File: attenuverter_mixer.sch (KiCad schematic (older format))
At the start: 77 parts, among them J0 Eurorack power, J1 In 1, J10 AudioJack1_SwitchT, J2 Out 1, J3 AudioJack1_SwitchT, J4 Out 2, J5 AudioJack1_SwitchT, J6 Out 3, J7 AudioJack1_SwitchT, J8 Out 4, J9 AudioJack1_SwitchT, U1 TL074, U2 TL074, U3 TL074

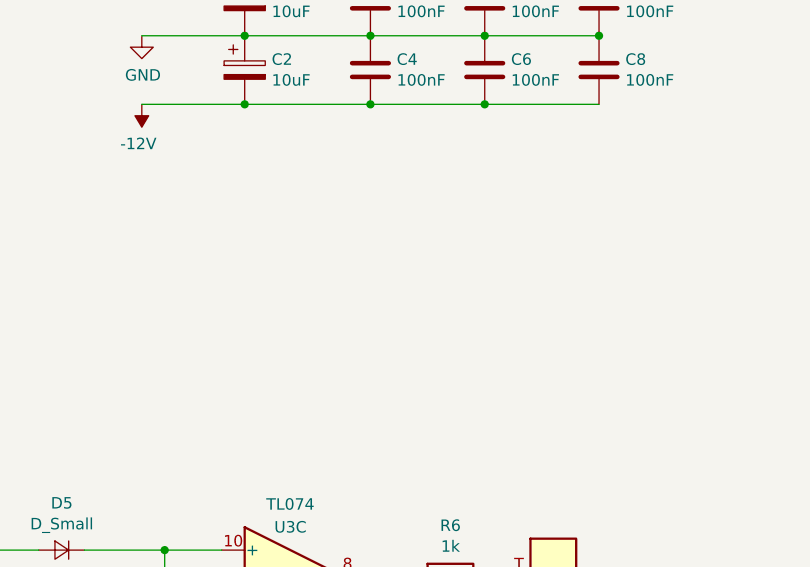
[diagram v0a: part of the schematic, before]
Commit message: Add the missing 5v voltage reference
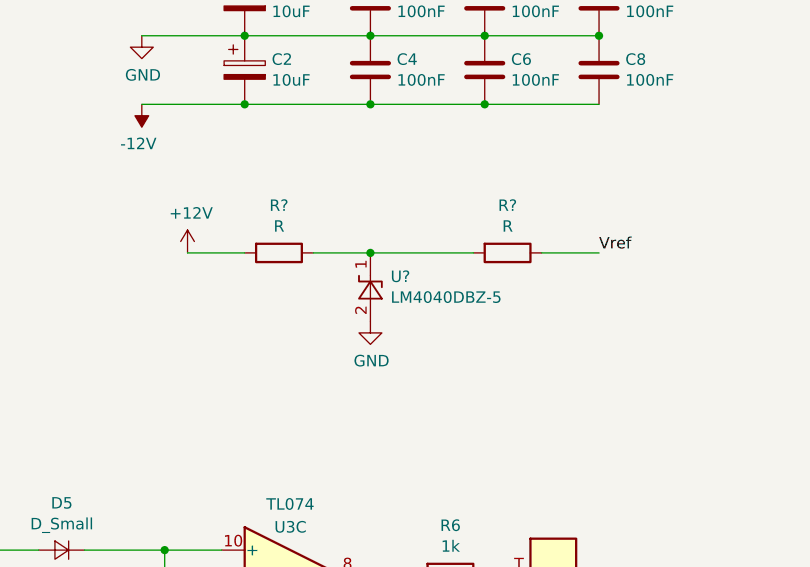
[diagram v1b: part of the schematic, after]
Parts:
- added R? (x2): R, symbol Device:R
- added U?: LM4040DBZ-5, Package_TO_SOT_SMD:SOT-23, symbol Reference_Voltage:LM4040DBZ-5
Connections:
- net +12V: now also R?.2
- net GND: now also U?.2 (A)
- net Vref: now also R?.1
- new net: R?.1, R?.2, U?.1 (K)
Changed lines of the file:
@@
 EESchema Schematic File Version 4
+LIBS:attenuverter_mixer-cache
 EELAYER 30 0
 EELAYER END
@@
 	0    -1   -1   0
 $EndComp
+$Comp
+L Reference_Voltage:LM4040DBZ-5 U?
+U 1 1 5D806F7C
+P 9350 3300
+F 0 "U?" V 9396 3212 50  0000 R CNN
+F 1 "LM4040DBZ-5" V 9305 3212 50  0000 R CNN
+F 2 "Package_TO_SOT_SMD:SOT-23" H 9350 3100 50  0001 C CIN
+F 3 "http://www.ti.com/lit/ds/symlink/lm4040-n.pdf" H 9350 3300 50  0001 C CIN
+	1    9350 3300
+	0    -1   -1   0
+$EndComp
+$Comp
+L power:GND #PWR?
+U 1 1 5D83B38C
+P 9350 3450
+F 0 "#PWR?" H 9350 3200 50  0001 C CNN
+F 1 "GND" H 9355 3277 50  0000 C CNN
+F 2 "" H 9350 3450 50  0001 C CNN
+F 3 "" H 9350 3450 50  0001 C CNN
+	1    9350 3450
+	1    0    0    -1
+$EndComp
+$Comp
+L power:+12V #PWR?
+U 1 1 5D851100
+P 8550 3150
+F 0 "#PWR?" H 8550 3000 50  0001 C CNN
+F 1 "+12V" H 8565 3323 50  0000 C CNN
+F 2 "" H 8550 3150 50  0001 C CNN
+F 3 "" H 8550 3150 50  0001 C CNN
+	1    8550 3150
+	1    0    0    -1
+$EndComp
+$Comp
+L Device:R R?
+U 1 1 5D89B833
+P 8950 3150
+F 0 "R?" V 8743 3150 50  0000 C CNN
+F 1 "R" V 8834 3150 50  0000 C CNN
+F 2 "" V 8880 3150 50  0001 C CNN
+F 3 "~" H 8950 3150 50  0001 C CNN
+	1    8950 3150
+	0    1    1    0
+$EndComp
+Wire Wire Line
+	8800 3150 8550 3150
+Wire Wire Line
+	9100 3150 9350 3150
+$Comp
+L Device:R R?
+U 1 1 5D8BBE6D
+P 9950 3150
+F 0 "R?" V 9743 3150 50  0000 C CNN
+F 1 "R" V 9834 3150 50  0000 C CNN
+F 2 "" V 9880 3150 50  0001 C CNN
+F 3 "~" H 9950 3150 50  0001 C CNN
+	1    9950 3150
+	0    1    1    0
+$EndComp
+Wire Wire Line
+	9350 3150 9800 3150
+Connection ~ 9350 3150
+Text Label 10350 3150 0    50   ~ 0
+Vref
+Wire Wire Line
+	10100 3150 10350 3150
 $EndSCHEMATC

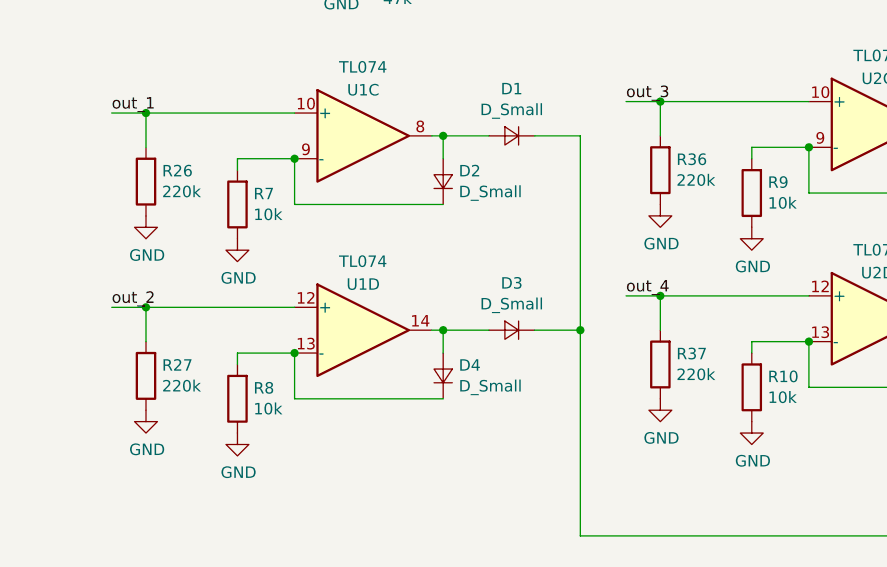
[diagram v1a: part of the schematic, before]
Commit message: Adjust peaks pull down resistors up to 1M
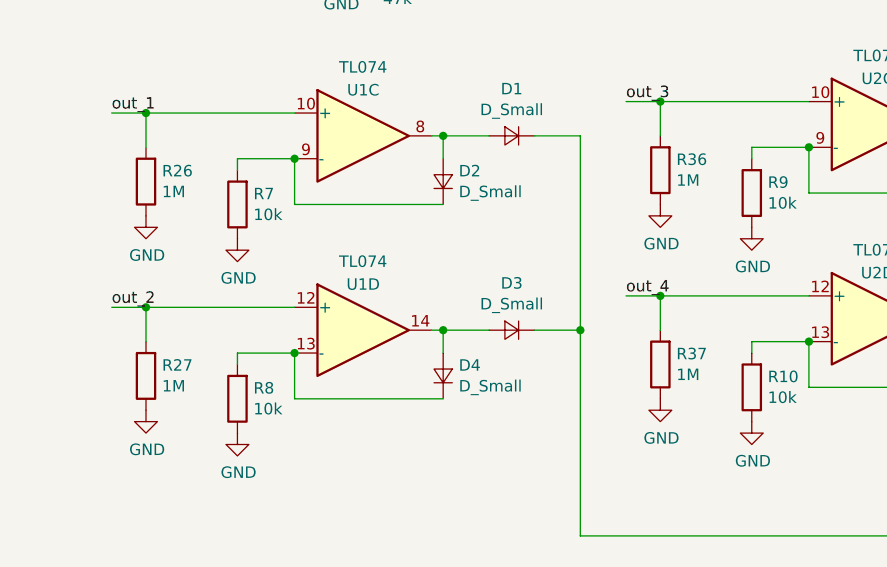
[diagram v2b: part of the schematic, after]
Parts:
- R26, R27, R36, R37: value 220k -> 1M
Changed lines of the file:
@@
 P 4150 4700
 F 0 "R26" H 4080 4654 50  0000 R CNN
-F 1 "220k" H 4080 4745 50  0000 R CNN
+F 1 "1M" H 4080 4745 50  0000 R CNN
 F 2 "" V 4080 4700 50  0001 C CNN
 F 3 "~" H 4150 4700 50  0001 C CNN
@@
 P 4150 5550
 F 0 "R27" H 4080 5504 50  0000 R CNN
-F 1 "220k" H 4080 5595 50  0000 R CNN
+F 1 "1M" H 4080 5595 50  0000 R CNN
 F 2 "" V 4080 5550 50  0001 C CNN
 F 3 "~" H 4150 5550 50  0001 C CNN
@@
 P 6400 4650
 F 0 "R36" H 6330 4604 50  0000 R CNN
-F 1 "220k" H 6330 4695 50  0000 R CNN
+F 1 "1M" H 6330 4695 50  0000 R CNN
 F 2 "" V 6330 4650 50  0001 C CNN
 F 3 "~" H 6400 4650 50  0001 C CNN
@@
 P 6400 5500
 F 0 "R37" H 6330 5454 50  0000 R CNN
-F 1 "220k" H 6330 5545 50  0000 R CNN
+F 1 "1M" H 6330 5545 50  0000 R CNN
 F 2 "" V 6330 5500 50  0001 C CNN
 F 3 "~" H 6400 5500 50  0001 C CNN

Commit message: assorted updates
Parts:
- removed D1, D2, D3, D4, D5, D6, D7, D8: D_Small, symbol Device:D_Small
- removed unit 2 of U1
- removed unit 3 of U1
- removed unit 4 of U1
- removed unit 1 of U2
- removed unit 2 of U2
- removed unit 3 of U2
- removed unit 4 of U2
- removed unit 3 of U3
- removed unit 5 of U3
- removed unit 4 of U3
- added C16, C9: 100nF, Capacitor_THT:C_Disc_D3.0mm_W1.6mm_P2.50mm, symbol Device:C
- added D1, D12, D13, D18, D2, D3, D4, D5, D6, D7: D_TVS, Diode_THT:D_DO-15_P12.70mm_Horizontal, symbol Device:D_TVS
- added D10, D11, D14, D15, D8, D9: 1N4148, Diode_THT:D_DO-35_SOD27_P7.62mm_Horizontal, symbol Diode:1N4148
- added D16, D17: 1N5817, Diode_THT:D_DO-41_SOD81_P10.16mm_Horizontal, symbol Device:D_Schottky
- added R38: 47k, Resistor_THT:R_Axial_DIN0207_L6.3mm_D2.5mm_P10.16mm_Horizontal, symbol Device:R
- added R39, R40, R41, R42: 100k, Resistor_THT:R_Axial_DIN0207_L6.3mm_D2.5mm_P10.16mm_Horizontal, symbol Device:R
- added R43, R44, R48: 330R, Resistor_THT:R_Axial_DIN0309_L9.0mm_D3.2mm_P12.70mm_Horizontal, symbol Device:R
- added R45, R46: 220k, Resistor_THT:R_Axial_DIN0207_L6.3mm_D2.5mm_P10.16mm_Horizontal, symbol Device:R
- added RV5, RV6: 100k, Potentiometer_THT:Potentiometer_Alpha_RD901F-40-00D_Single_Vertical, symbol Device:R_POT
- added unit 2 of U1
- added unit 2 of U2
- added unit 1 of U2
- added U3, U4: TL072, Package_SO:SOIC-8_3.9x4.9mm_P1.27mm, symbol Amplifier_Operational:TL072
- added unit 4 of U5
- added unit 5 of U5
- added unit 3 of U5
- C1, C2: footprint (none) -> Capacitor_THT:CP_Radial_D5.0mm_P2.00mm
- C10, C14, C15: footprint (none) -> Capacitor_THT:C_Disc_D3.0mm_W2.0mm_P2.50mm
- C11, C12, C13: value 18pF -> 100nF; footprint (none) -> Capacitor_THT:C_Disc_D3.0mm_W1.6mm_P2.50mm
- C3, C4, C8: footprint (none) -> Capacitor_THT:C_Disc_D3.0mm_W1.6mm_P2.50mm
- C5, C6, C7: value 100nF -> 18pF; footprint (none) -> Capacitor_THT:C_Disc_D3.0mm_W2.0mm_P2.50mm
- J0: footprint Connector_IDC:IDC-Header_2x05_P2.54mm_Vertical_Lock -> Connector_PinSocket_2.54mm:PinSocket_2x05_P2.54mm_Vertical
- J1: value In 1 -> Input; footprint (none) -> kicad_libraries:Jack_3.5mm_QingPu_WQP-PJ398SM_Vertical_CircularHoles
- J10: value AudioJack1_SwitchT -> Or out; footprint (none) -> kicad_libraries:Jack_3.5mm_QingPu_WQP-PJ398SM_Vertical_CircularHoles
- J2: value Out 1 -> Out; footprint (none) -> kicad_libraries:Jack_3.5mm_QingPu_WQP-PJ398SM_Vertical_CircularHoles
- J3, J5: value AudioJack1_SwitchT -> Input; footprint (none) -> kicad_libraries:Jack_3.5mm_QingPu_WQP-PJ398SM_Vertical_CircularHoles
- J4: value Out 2 -> Out; footprint (none) -> kicad_libraries:Jack_3.5mm_QingPu_WQP-PJ398SM_Vertical_CircularHoles
- J6: value Out 3 -> Input; footprint (none) -> kicad_libraries:Jack_3.5mm_QingPu_WQP-PJ398SM_Vertical_CircularHoles
- J7: value AudioJack1_SwitchT -> Out; footprint (none) -> kicad_libraries:Jack_3.5mm_QingPu_WQP-PJ398SM_Vertical_CircularHoles
- J8: value Out 4 -> Out; footprint (none) -> kicad_libraries:Jack_3.5mm_QingPu_WQP-PJ398SM_Vertical_CircularHoles
- J9: value AudioJack1_SwitchT -> Sum out; footprint (none) -> kicad_libraries:Jack_3.5mm_QingPu_WQP-PJ398SM_Vertical_CircularHoles
- R1, R5: value 1k -> 330R; footprint (none) -> Resistor_THT:R_Axial_DIN0309_L9.0mm_D3.2mm_P12.70mm_Horizontal
- R10, R9: value 10k -> 47k; footprint (none) -> Resistor_THT:R_Axial_DIN0207_L6.3mm_D2.5mm_P10.16mm_Horizontal
- R11, R12, R13, R14, R22: value 100k -> 220k; footprint (none) -> Resistor_THT:R_Axial_DIN0207_L6.3mm_D2.5mm_P10.16mm_Horizontal
- R15, R16, R19, R20, R21, R23, R24, R25, R32: footprint (none) -> Resistor_THT:R_Axial_DIN0207_L6.3mm_D2.5mm_P10.16mm_Horizontal
- R17, R18, R28, R29, R31: value 47k -> 100k; footprint (none) -> Resistor_THT:R_Axial_DIN0207_L6.3mm_D2.5mm_P10.16mm_Horizontal
- R2, R3, R4, R6: value 1k -> 100k; footprint (none) -> Resistor_THT:R_Axial_DIN0207_L6.3mm_D2.5mm_P10.16mm_Horizontal
- R26, R27: value 1M -> 100k; footprint (none) -> Resistor_THT:R_Axial_DIN0207_L6.3mm_D2.5mm_P10.16mm_Horizontal
- R30: value 47k -> 330R; footprint (none) -> Resistor_THT:R_Axial_DIN0309_L9.0mm_D3.2mm_P12.70mm_Horizontal
- R33: value 100k -> 100R; footprint (none) -> Resistor_THT:R_Axial_DIN0204_L3.6mm_D1.6mm_P7.62mm_Horizontal
- R34, R35: value 100k -> 47k; footprint (none) -> Resistor_THT:R_Axial_DIN0207_L6.3mm_D2.5mm_P10.16mm_Horizontal
- R36: value 1M -> 100R; footprint (none) -> Resistor_THT:R_Axial_DIN0204_L3.6mm_D1.6mm_P7.62mm_Horizontal
- R37: value 1M -> 47k; footprint (none) -> Resistor_THT:R_Axial_DIN0207_L6.3mm_D2.5mm_P10.16mm_Horizontal
- R47, R49: renamed from R?; footprint (none) -> Resistor_THT:R_Axial_DIN0309_L9.0mm_D3.2mm_P12.70mm_Horizontal
- R7, R8: value 10k -> 100R; footprint (none) -> Resistor_THT:R_Axial_DIN0204_L3.6mm_D1.6mm_P7.62mm_Horizontal
- RV1, RV2, RV3, RV4: footprint (none) -> Potentiometer_THT:Potentiometer_Alpha_RD901F-40-00D_Single_Vertical
- U1, U2: value TL074 -> TL072; footprint (none) -> Package_SO:SOIC-8_3.9x4.9mm_P1.27mm; symbol Amplifier_Operational:TL074 -> Amplifier_Operational:TL072
- U5: renamed from U3; footprint (none) -> Package_SO:SOIC-14_3.9x8.7mm_P1.27mm
- U6: renamed from U?; value LM4040DBZ-5 -> LM4040CIZ-5.0; footprint Package_TO_SOT_SMD:SOT-23 -> Package_TO_SOT_THT:TO-92_Inline
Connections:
- net +12V: now also C11.1, C13.1, C8.1, U1.8 (V+), U2.8 (V+), D17.1 (K), U3.8 (V+), U4.8 (V+), U5.4 (V+); no longer C5.1, C7.1, J0.5 (Pin_5), J0.6 (Pin_6), U1.4 (V+), U2.4 (V+)
- net -12V: now also C12.2, U1.4 (V-), U2.4 (V-), C16.2, C9.2, D16.2 (A), R45.2, R46.2, U3.4 (V-), U4.4 (V-), U5.11 (V-); no longer C6.2, C8.2, J0.1 (Pin_1), J0.10 (Pin_10), U1.11 (V-), U2.11 (V-)
- net GND: now also C11.2, C12.1, C13.2, C8.2, J0.2 (Pin_2), J0.4 (Pin_4), J0.7 (Pin_7), J0.9 (Pin_9), J1.TN, J3.TN, R32.1, R35.1, C16.1, C9.1, D14.2 (A), R38.1, RV5.3, RV6.3, U5.12 (+); no longer C5.2, C6.1, C7.2, C8.1, J1.S, J10.S, J2.S, J3.S, J4.S, J5.S, J6.S, J7.S, J8.S, J9.S, R18.1, R26.1, R27.1, R29.1, R36.1, R37.1, R7.1, R8.1, R9.1
- net Vref: now also J6.TN, R2.2, R3.2, RV2.1, RV3.1; no longer J1.TN, J3.TN, J7.TN
- net out_1: now also D8.2 (A); no longer R26.2
- net out_2: now also D9.2 (A); no longer R27.2
- net out_3: now also J7.TN, D10.2 (A); no longer J6.TN, R36.2
- net out_4: now also D11.2 (A); no longer R37.2
- net at R23.1, U1.1: now also C10.2, R24.2; no longer C10.1, R1.2
- net at R20.1, R23.2, U1.2 (-): now also C10.1; no longer C10.2
- net at R15.1, R20.2, RV1.1: now also R7.1, D1.1 (A1); no longer J1.T
- net at J2.T, R1.1: now also D3.1 (A1)
- net at J5.T, R33.2: no longer R30.1, RV4.1
- net at R3.1: now also R6.1, U3.6 (-); no longer J6.T
- net at J4.T: now also R30.1, D4.1 (A1); no longer R2.1
- net at R4.1: now also R2.1, U1.6 (-); no longer J8.T
- net at C14.1, R22.1, U5.1: now also R19.1; no longer R19.2
- net at J9.T, R5.1: now also D7.1 (A1)
- net at C15.2, R25.2, U5.6 (-): now also R19.2; no longer R19.1
- net at R7.2: now also J1.T
- net at R8.2: now also J3.T
- net at R9.2: now also R10.2, RV4.2, U3.3 (+)
- net at R6.2: now also R18.2, U3.7
- net at J10.T: now also D18.1 (A1), R48.1; no longer R6.1
- net GNDPWR: now reaches J0.3 (Pin_3), J0.8 (Pin_8)
- net GNDPWR: now also J1.S, J10.S, J2.S, J3.S, J4.S, J5.S, J6.S, J7.S, J8.S, J9.S, D1.2 (A2), D12.2 (A2), D13.2 (A2), D18.2 (A2), D2.2 (A2), D3.2 (A2), D4.2 (A2), D5.2 (A2), D6.2 (A2), D7.2 (A2)
- new net: R1.2, R28.2, U2.1
- new net: C5.1, R21.1, R26.2, U3.2 (-)
- new net: D2.1 (A1), R21.2, R8.1, R9.1, RV4.1
- new net: C5.2, R26.1, R27.2, U3.1
- new net: R29.2, R30.2, U2.7
- new net: RV3.2, U3.5 (+)
- new net: R18.1, R27.1, U2.5 (+)
- new net: R29.1, R32.2, U2.6 (-)
- new net: D16.1 (K), J0.1 (Pin_1), J0.10 (Pin_10)
- new net: D17.2 (A), J0.5 (Pin_5), J0.6 (Pin_6)
- new net: U5.13 (-), U5.14
- new net: C6.1, R39.1, R41.2, U4.2 (-)
- new net: D5.1 (A1), R33.1, R34.1, R39.2, RV5.1
- new net: C6.2, R41.1, R43.2, U4.1
- new net: R34.2, R35.2, RV5.2, U4.3 (+)
- new net: D12.1 (A1), J7.T, R43.1
- new net: D10.1 (K), D11.1 (K), D14.1 (K), D8.1 (K), D9.1 (K), R45.1, U5.10 (+)
- new net: D15.2 (A), R48.2, U5.8
- new net: D15.1 (K), R46.1, U5.9 (-)
- new net: RV2.2, U1.5 (+)
- new net: R28.1, R31.2, U2.2 (-)
- new net: R17.1, R24.1, U2.3 (+)
- new net: R17.2, R4.2, U1.7
- new net: J6.T, R36.2
- new net: C7.1, R40.1, R42.2, U4.6 (-)
- new net: D6.1 (A1), R36.1, R37.1, R40.2, RV6.1
- new net: C7.2, R42.1, R44.2, U4.7
- new net: R37.2, R38.2, RV6.2, U4.5 (+)
- new net: D13.1 (A1), J8.T, R44.1
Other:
- moved on the sheet: C1, C10, C14, C15, C2, C3, C4, J0, J1, J2, J9, R1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

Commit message: Remove TVS diodes from i/o
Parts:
- removed D1, D12, D13, D18, D2, D3, D4, D7: D_TVS, Diode_THT:D_DO-15_P12.70mm_Horizontal, symbol Device:D_TVS
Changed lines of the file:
@@
 	10600 3800 10850 3800
-$Comp
-L Device:D_TVS D3
-U 1 1 5D9F5BE0
-P 4000 1050
-F 0 "D3" V 3954 1129 50  0000 L CNN
-F 1 "D_TVS" V 4045 1129 50  0000 L CNN
-F 2 "Diode_THT:D_DO-15_P12.70mm_Horizontal" H 4000 1050 50  0001 C CNN
-F 3 "~" H 4000 1050 50  0001 C CNN
-	1    4000 1050
-	0    1    1    0
-$EndComp
-$Comp
-L Device:D_TVS D1
-U 1 1 5DA043FF
-P 1200 1800
-F 0 "D1" V 1150 1600 50  0000 L CNN
-F 1 "D_TVS" V 1250 1500 50  0000 L CNN
-F 2 "Diode_THT:D_DO-15_P12.70mm_Horizontal" H 1200 1800 50  0001 C CNN
-F 3 "~" H 1200 1800 50  0001 C CNN
-	1    1200 1800
-	0    1    1    0
-$EndComp
 $Comp
 L Device:D_Schottky D16
@@
 	1    0    0    -1
 $EndComp
-$Comp
-L power:GNDPWR #PWR0111
-U 1 1 5DBA6434
-P 1200 1950
-F 0 "#PWR0111" H 1200 1750 50  0001 C CNN
-F 1 "GNDPWR" H 1204 1796 50  0000 C CNN
-F 2 "" H 1200 1900 50  0001 C CNN
-F 3 "" H 1200 1900 50  0001 C CNN
-	1    1200 1950
-	1    0    0    -1
-$EndComp
-$Comp
-L power:GNDPWR #PWR0112
-U 1 1 5DBA6A42
-P 4000 1200
-F 0 "#PWR0112" H 4000 1000 50  0001 C CNN
-F 1 "GNDPWR" H 4004 1046 50  0000 C CNN
-F 2 "" H 4000 1150 50  0001 C CNN
-F 3 "" H 4000 1150 50  0001 C CNN
-	1    4000 1200
-	1    0    0    -1
-$EndComp
 Wire Wire Line
 	3250 1650 3300 1650
@@
 Wire Wire Line
 	1950 1250 1950 1550
-Connection ~ 1700 1550
-Wire Wire Line
-	1200 1650 1200 1550
-Wire Wire Line
-	1200 1550 1700 1550
-Wire Wire Line
-	4000 850  4000 900
 $Comp
 L attenuverter_mixer:AudioJack1_SwitchT J5
@@
 	7800 2050 7800 2000
 $Comp
-L Device:D_TVS D12
-U 1 1 5DBA22E7
-P 8100 1150
-F 0 "D12" V 8054 1229 50  0000 L CNN
-F 1 "D_TVS" V 8145 1229 50  0000 L CNN
-F 2 "Diode_THT:D_DO-15_P12.70mm_Horizontal" H 8100 1150 50  0001 C CNN
-F 3 "~" H 8100 1150 50  0001 C CNN
-	1    8100 1150
-	0    1    1    0
-$EndComp
-$Comp
 L Device:D_TVS D5
 U 1 1 5DBA22F1
@@
 F 3 "" H 5450 2050 50  0001 C CNN
 	1    5450 2100
-	1    0    0    -1
-$EndComp
-$Comp
-L power:GNDPWR #PWR0119
-U 1 1 5DBA2319
-P 8100 1300
-F 0 "#PWR0119" H 8100 1100 50  0001 C CNN
-F 1 "GNDPWR" H 8104 1146 50  0000 C CNN
-F 2 "" H 8100 1250 50  0001 C CNN
-F 3 "" H 8100 1250 50  0001 C CNN
-	1    8100 1300
 	1    0    0    -1
 $EndComp
@@
 	7900 1250 7900 950
 Wire Wire Line
-	7900 950  8100 950
-Wire Wire Line
-	8100 950  8100 1000
-Connection ~ 7900 950
-Wire Wire Line
 	9800 650  9800 600
 Wire Wire Line
@@
 	-1   0    0    -1
 $EndComp
-Wire Wire Line
-	10500 5350 10300 5350
 NoConn ~ 10500 5450
-$Comp
-L Device:D_TVS D18
-U 1 1 5DF5B69B
-P 10300 5700
-F 0 "D18" V 10254 5779 50  0000 L CNN
-F 1 "D_TVS" V 10345 5779 50  0000 L CNN
-F 2 "Diode_THT:D_DO-15_P12.70mm_Horizontal" H 10300 5700 50  0001 C CNN
-F 3 "~" H 10300 5700 50  0001 C CNN
-	1    10300 5700
-	0    1    1    0
-$EndComp
-$Comp
-L power:GNDPWR #PWR0121
-U 1 1 5DF5B6A5
-P 10300 6050
-F 0 "#PWR0121" H 10300 5850 50  0001 C CNN
-F 1 "GNDPWR" H 10304 5896 50  0000 C CNN
-F 2 "" H 10300 6000 50  0001 C CNN
-F 3 "" H 10300 6000 50  0001 C CNN
-	1    10300 6050
-	1    0    0    -1
-$EndComp
-Wire Wire Line
-	10300 5550 10300 5350
-Connection ~ 10300 5350
-Wire Wire Line
-	10300 5350 10150 5350
-Wire Wire Line
-	10700 5850 10300 5850
 Wire Wire Line
 	10700 5650 10700 5850
@@
 	3450 1750 3900 1750
 Wire Wire Line
-	3450 850  3450 1750
-Wire Wire Line
-	3450 850  4000 850
-Connection ~ 3450 1750
-Wire Wire Line
 	3500 7400 3200 7400
 Wire Wire Line
@@
 Wire Wire Line
 	3950 7000 3950 7200
-Wire Wire Line
-	5700 6900 5850 6900
-$Comp
-L Device:D_TVS D7
-U 1 1 5E5B15E4
-P 5850 7150
-F 0 "D7" V 5804 7229 50  0000 L CNN
-F 1 "D_TVS" V 5895 7229 50  0000 L CNN
-F 2 "Diode_THT:D_DO-15_P12.70mm_Horizontal" H 5850 7150 50  0001 C CNN
-F 3 "~" H 5850 7150 50  0001 C CNN
-	1    5850 7150
-	0    1    1    0
-$EndComp
-Wire Wire Line
-	5850 7000 5850 6900
-Connection ~ 5850 6900
-Wire Wire Line
-	5850 6900 6200 6900
-Wire Wire Line
-	6400 7500 6400 7350
-Wire Wire Line
-	5850 7300 5850 7350
-Wire Wire Line
-	5850 7350 6400 7350
-Connection ~ 6400 7350
-Wire Wire Line
-	6400 7350 6400 7200
 $Comp
 L attenuverter_mixer:AudioJack1_SwitchT J6
@@
 	7800 4300 7800 4250
 $Comp
-L Device:D_TVS D13
-U 1 1 5E627777
-P 8100 3400
-F 0 "D13" V 8054 3479 50  0000 L CNN
-F 1 "D_TVS" V 8145 3479 50  0000 L CNN
-F 2 "Diode_THT:D_DO-15_P12.70mm_Horizontal" H 8100 3400 50  0001 C CNN
-F 3 "~" H 8100 3400 50  0001 C CNN
-	1    8100 3400
-	0    1    1    0
-$EndComp
-$Comp
 L Device:D_TVS D6
 U 1 1 5E627781
@@
 F 3 "" H 5450 4300 50  0001 C CNN
 	1    5450 4350
-	1    0    0    -1
-$EndComp
-$Comp
-L power:GNDPWR #PWR0137
-U 1 1 5E6277A9
-P 8100 3550
-F 0 "#PWR0137" H 8100 3350 50  0001 C CNN
-F 1 "GNDPWR" H 8104 3396 50  0000 C CNN
-F 2 "" H 8100 3500 50  0001 C CNN
-F 3 "" H 8100 3500 50  0001 C CNN
-	1    8100 3550
 	1    0    0    -1
 $EndComp
@@
 	7900 3500 7900 3200
 Wire Wire Line
-	7900 3200 8100 3200
-Wire Wire Line
-	8100 3200 8100 3250
-Connection ~ 7900 3200
-Wire Wire Line
 	3550 6800 3600 6800
 Wire Wire Line
@@
 	4000 4700 4000 4650
 $Comp
-L Device:D_TVS D4
-U 1 1 5D9AA64D
-P 4100 3850
-F 0 "D4" V 4054 3929 50  0000 L CNN
-F 1 "D_TVS" V 4145 3929 50  0000 L CNN
-F 2 "Diode_THT:D_DO-15_P12.70mm_Horizontal" H 4100 3850 50  0001 C CNN
-F 3 "~" H 4100 3850 50  0001 C CNN
-	1    4100 3850
-	0    1    1    0
-$EndComp
-$Comp
-L Device:D_TVS D2
-U 1 1 5D9AA657
-P 1300 4600
-F 0 "D2" V 1250 4400 50  0000 L CNN
-F 1 "D_TVS" V 1350 4300 50  0000 L CNN
-F 2 "Diode_THT:D_DO-15_P12.70mm_Horizontal" H 1300 4600 50  0001 C CNN
-F 3 "~" H 1300 4600 50  0001 C CNN
-	1    1300 4600
-	0    1    1    0
-$EndComp
-$Comp
 L power:GNDPWR #PWR0141
 U 1 1 5D9AA661
@@
 F 3 "" H 4200 4800 50  0001 C CNN
 	1    4200 4850
-	1    0    0    -1
-$EndComp
-$Comp
-L power:GNDPWR #PWR0143
-U 1 1 5D9AA675
-P 1300 4750
-F 0 "#PWR0143" H 1300 4550 50  0001 C CNN
-F 1 "GNDPWR" H 1304 4596 50  0000 C CNN
-F 2 "" H 1300 4700 50  0001 C CNN
-F 3 "" H 1300 4700 50  0001 C CNN
-	1    1300 4750
-	1    0    0    -1
-$EndComp
-$Comp
-L power:GNDPWR #PWR0144
-U 1 1 5D9AA67F
-P 4100 4000
-F 0 "#PWR0144" H 4100 3800 50  0001 C CNN
-F 1 "GNDPWR" H 4104 3846 50  0000 C CNN
-F 2 "" H 4100 3950 50  0001 C CNN
-F 3 "" H 4100 3950 50  0001 C CNN
-	1    4100 4000
 	1    0    0    -1
 $EndComp
@@
 Wire Wire Line
 	2050 4050 2050 4350
-Connection ~ 1800 4350
-Wire Wire Line
-	1300 4450 1300 4350
-Wire Wire Line
-	1300 4350 1800 4350
-Wire Wire Line
-	4100 3650 4100 3700
 $Comp
 L Device:R_POT RV3
@@
 Wire Wire Line
 	3550 4550 4000 4550
-Wire Wire Line
-	3550 3650 3550 4550
-Wire Wire Line
-	3550 3650 4100 3650
-Connection ~ 3550 4550
 $Comp
 L power:GND #PWR0146
@@
 	4100 2150 4100 2050
 Wire Wire Line
-	10300 6050 10300 5850
-Connection ~ 10300 5850
-Wire Wire Line
 	6300 5400 6300 5350
 Wire Wire Line
@@
 Wire Wire Line
 	6700 5350 6700 5400
+Wire Wire Line
+	6400 7200 6400 7500
+Wire Wire Line
+	5700 6900 6200 6900
+$Comp
+L power:GNDPWR #PWR0121
+U 1 1 5DF5B6A5
+P 10700 5850
+F 0 "#PWR0121" H 10700 5650 50  0001 C CNN
+F 1 "GNDPWR" H 10704 5696 50  0000 C CNN
+F 2 "" H 10700 5800 50  0001 C CNN
+F 3 "" H 10700 5800 50  0001 C CNN
+	1    10700 5850
+	1    0    0    -1
+$EndComp
+Wire Wire Line
+	10150 5350 10500 5350
 $EndSCHEMATC
